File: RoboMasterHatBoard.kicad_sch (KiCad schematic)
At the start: 21 parts, among them J1 Conn_01x08_Socket, J10 Conn_01x02_Pin, J11 Conn_01x03_Pin, J12 Conn_01x05_Pin, J13 Conn_01x05_Pin, J14 Conn_01x03_Pin, J15 Conn_01x03_Pin, J16 Conn_01x02_Pin, J2 Conn_01x08_Socket, J3 Conn_01x08_Socket, J4 Conn_01x08_Socket, J5 Conn_01x08_Socket, J6 Conn_01x08_Socket, J7 Conn_01x10_Socket, J8 Conn_01x10_Socket, J9 Conn_01x02_Pin, U1 AMS1117-3.3

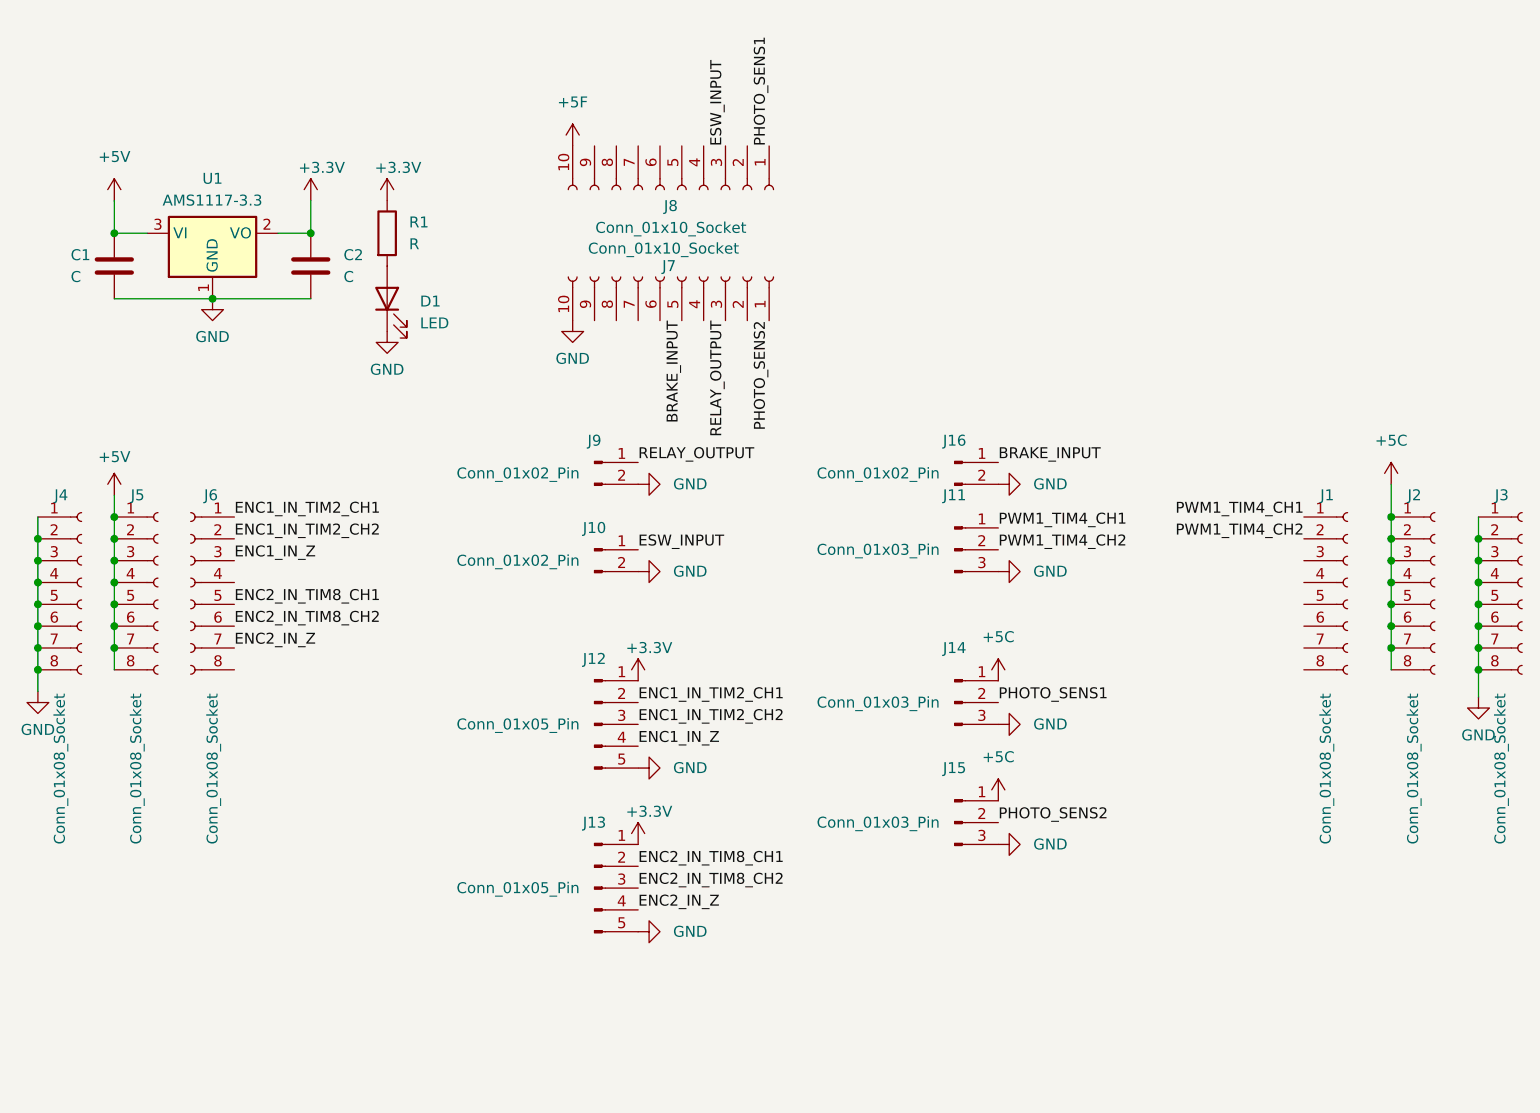
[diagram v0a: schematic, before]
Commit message: 撃破入力ピンを追加
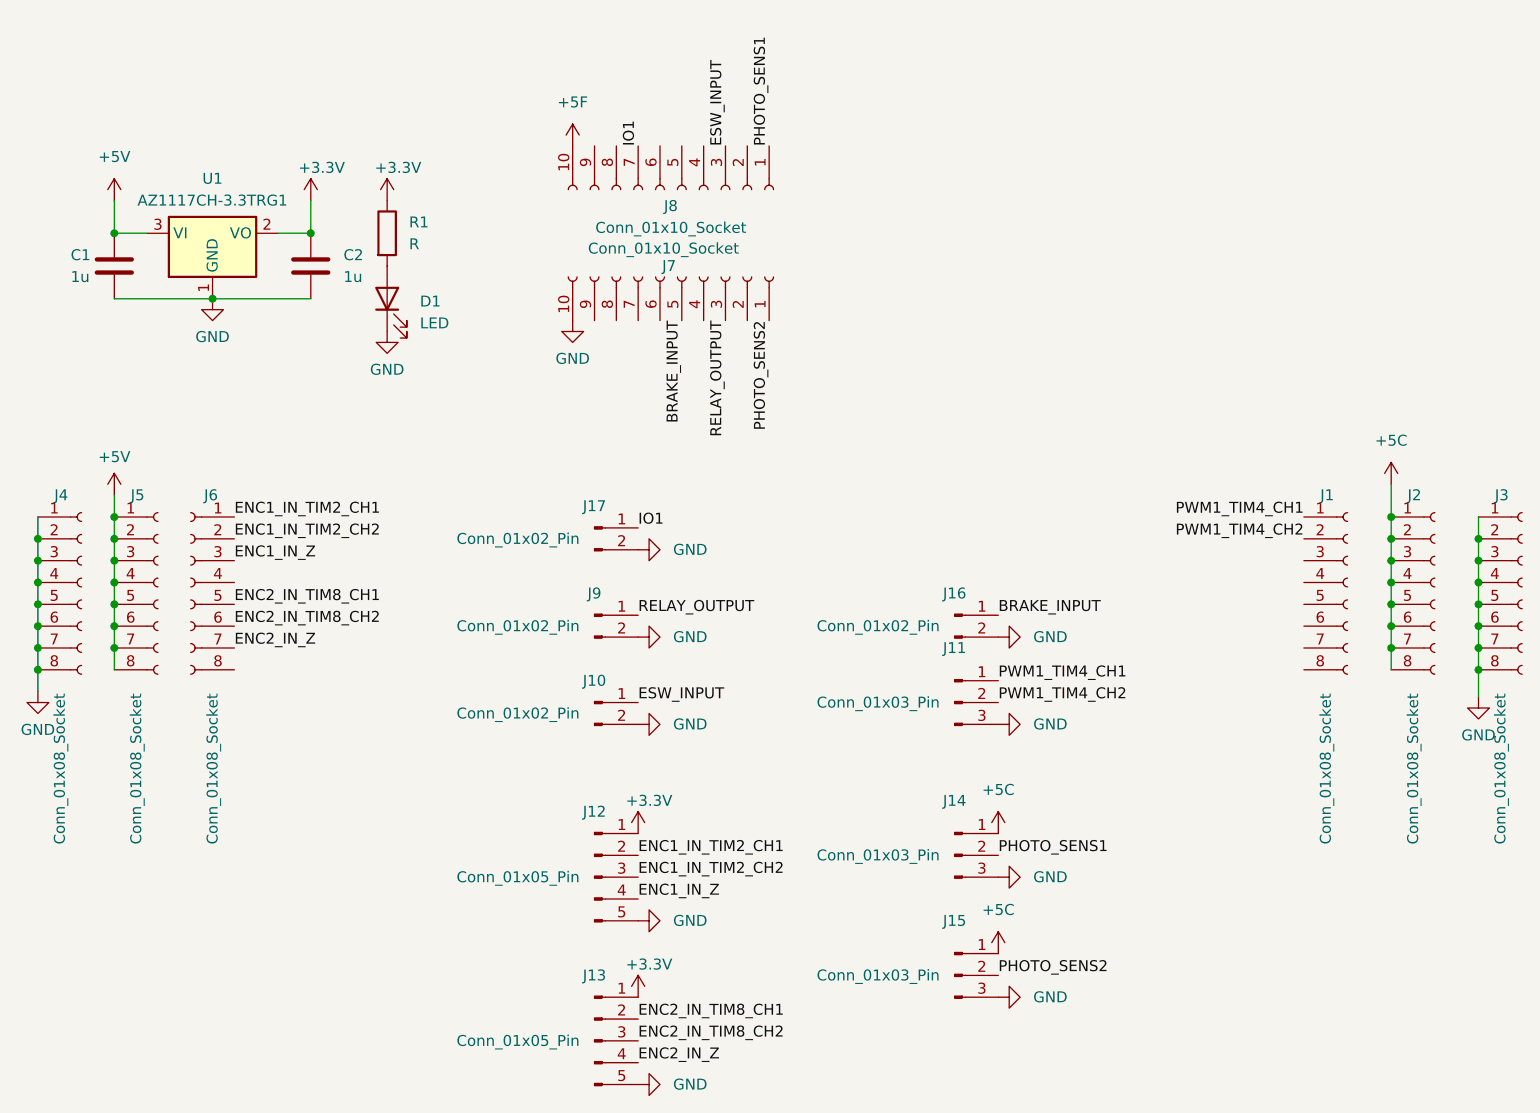
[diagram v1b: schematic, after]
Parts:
- added J17: Conn_01x02_Pin, Connector_JST:JST_XH_B2B-XH-A_1x02_P2.50mm_Vertical, symbol Connector:Conn_01x02_Pin
- C1, C2: value C -> 1u
- U1: value AMS1117-3.3 -> AZ1117CH-3.3TRG1; order_URL (none) -> https://akizukidenshi.com/catalog/g/gI-16155/
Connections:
- net GND: now also J17.2 (Pin_2)
- net IO1: now reaches J8.7 (Pin_7)
- net IO1: now also J17.1 (Pin_1)
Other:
- moved on the sheet: J10, J11, J12, J13, J14, J15, J16, J9
